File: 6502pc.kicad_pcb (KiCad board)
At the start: 2 copper layers, 32 parts, among them J1 DE9_Receptacle, J2 USB_B, J3 Conn_01x08_Pin, J4 Conn_01x08_Pin, J5 Conn_01x16_Socket, SW1 SW_Push, U1 W65C02SxP, U2 28C256, U3 CY62256-70PC, U4 W65C51NxP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

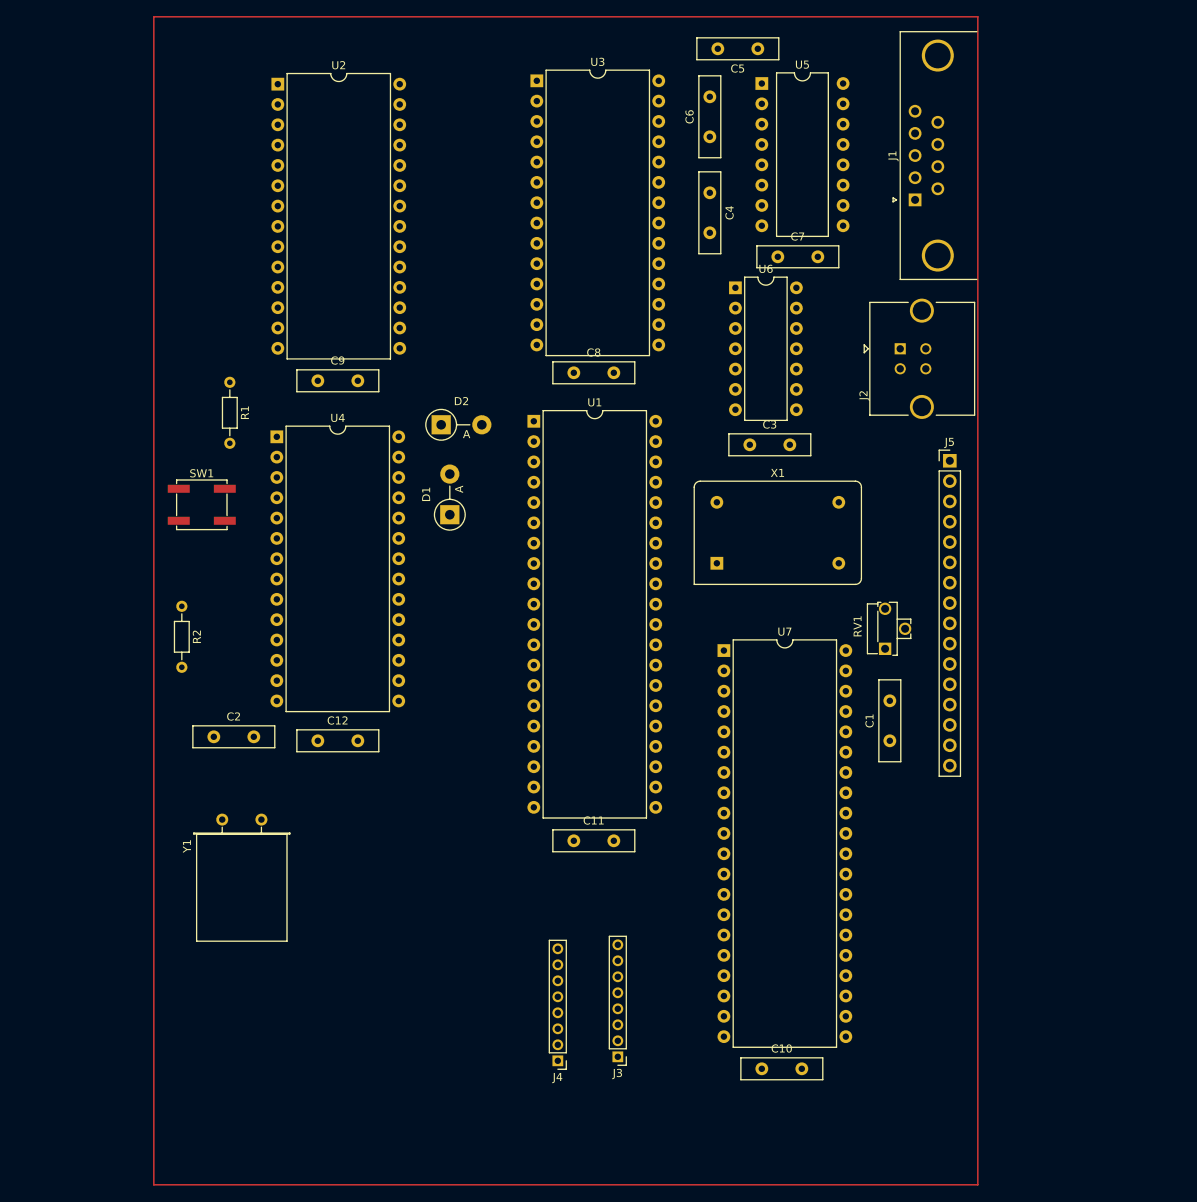
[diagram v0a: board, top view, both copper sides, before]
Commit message: Added Expansion
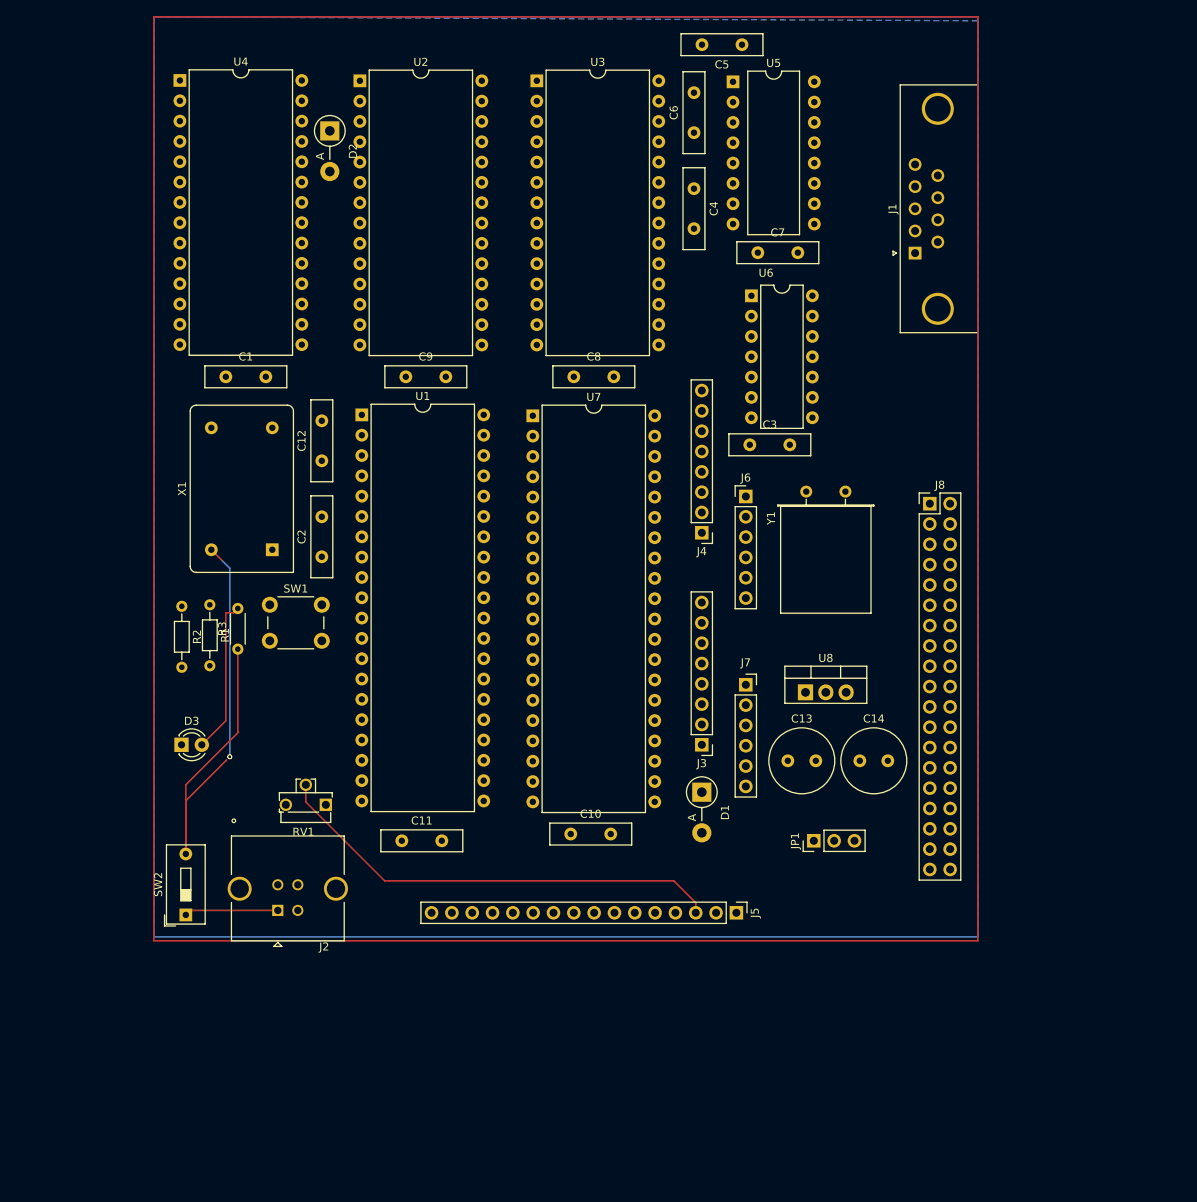
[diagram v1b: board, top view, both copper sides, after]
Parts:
- added C13: 100nF, Capacitor_THT:C_Radial_D8.0mm_H11.5mm_P3.50mm, F.Cu at (114.8, 118.0)
- added C14: 10uF, Capacitor_THT:C_Radial_D8.0mm_H11.5mm_P3.50mm, F.Cu at (123.8, 118.0)
- added D3: LED, LED_THT:LED_D3.0mm, F.Cu at (39.0, 116.0)
- added J6: SD-Card Board, Connector_PinHeader_2.54mm:PinHeader_1x06_P2.54mm_Vertical, F.Cu at (109.5, 85.0)
- added J7: FTDI Socket, Connector_PinSocket_2.54mm:PinSocket_1x06_P2.54mm_Vertical, F.Cu at (109.5, 108.5)
- added J8: Expansion / Diag Port, Connector_PinHeader_2.54mm:PinHeader_2x19_P2.54mm_Vertical, F.Cu at (132.5, 85.9)
- added JP1: SD/FTDI 3.3 or 5v, Connector_PinHeader_2.54mm:PinHeader_1x03_P2.54mm_Vertical, F.Cu at (118.0, 128.0)
- added R3: 220, Resistor_THT:R_Axial_DIN0204_L3.6mm_D1.6mm_P5.08mm_Horizontal, F.Cu at (46.0, 104.0)
- added SW2: SW_SPST, Button_Switch_THT:SW_DIP_SPSTx01_Slide_9.78x4.72mm_W7.62mm_P2.54mm, F.Cu at (39.5, 137.3)
- added U8: LM317_TO-220, Package_TO_SOT_THT:TO-220-3_Vertical, F.Cu at (117.0, 109.4)
- J1: value DE9_Receptacle -> DB9 Serial Port
- J3, J4: footprint Connector_PinHeader_2.00mm:PinHeader_1x08_P2.00mm_Vertical -> Connector_PinHeader_2.54mm:PinHeader_1x08_P2.54mm_Vertical
- SW1: value SW_Push -> Reset Switch; footprint Button_Switch_SMD:SW_SPST_EVPBF -> Button_Switch_THT:SW_PUSH_6mm
- moved J2 104.8 mm to (51.0, 136.7), turned to 180 degrees
- moved C1 94.7 mm to (44.5, 70.0), turned to 0 degrees
- moved Y1 83.7 mm to (117.0, 84.3)
- moved RV1 72.6 mm to (57.0, 123.5), turned to 180 degrees
- moved J4 68.4 mm to (104.0, 89.5)
- moved J5 62.5 mm to (108.3, 137.0), turned to -90 degrees
- moved X1 55.6 mm to (50.3, 91.6), turned to 90 degrees
- moved D1 46.9 mm to (104.0, 121.9), turned to -90 degrees
- moved U4 46.2 mm to (38.8, 33.0)
- moved J3 40.4 mm to (104.0, 116.0)
- moved D2 39.3 mm to (57.5, 39.3), turned to -90 degrees
- moved C10 37.8 mm to (87.6, 127.2)
- moved U7 37.8 mm to (82.9, 74.9)
- moved C12 35.0 mm to (56.5, 80.5), turned to 90 degrees
- moved R1 27.9 mm to (42.5, 98.5)
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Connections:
- net Net-(J4-Pin_2) renamed PA6
- net Net-(J4-Pin_3) renamed PA5
- net Net-(J4-Pin_4) renamed PA4
- net Net-(J4-Pin_5) renamed PA3
- net Net-(J4-Pin_6) renamed PA2
- net Net-(J4-Pin_7) renamed PA1
- net Net-(J4-Pin_8) renamed PA0
- J1 pad 4: unconnected-(J1-Pad4) -> Net-(J7-Pin_6)
- J1 pad 6: unconnected-(J1-Pad6) -> Net-(U4-~{DSR})
- J1 pad 7: unconnected-(J1-Pad7) -> Net-(U4-~{RTS})
- J1 pad 8: unconnected-(J1-Pad8) -> Net-(J7-Pin_2)
- J2 pad 1: VCC -> Net-(J2-VBUS)
- U4 pad 11: unconnected-(U4-~{DTR}-Pad11) -> Net-(J7-Pin_6)
- U4 pad 17: unconnected-(U4-~{DSR}-Pad17) -> Net-(U4-~{DSR})
- U4 pad 8: unconnected-(U4-~{RTS}-Pad8) -> Net-(U4-~{RTS})
- U4 pad 9: unconnected-(U4-~{CTS}-Pad9) -> Net-(J7-Pin_2)
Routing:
- net Net-(J5-Pin_3): track 0.00 -> 57.4 mm
- net VCC: track 0.00 -> 44.1 mm
- net (no net): track 0.00 -> 24.9 mm, vias 0 -> 3
- net Net-(D3-A): track 0.00 -> 19.5 mm
- net Net-(J2-VBUS): track 0.00 -> 11.7 mm
- added copper zone on B.Cu, net GND

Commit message: Added Expansion
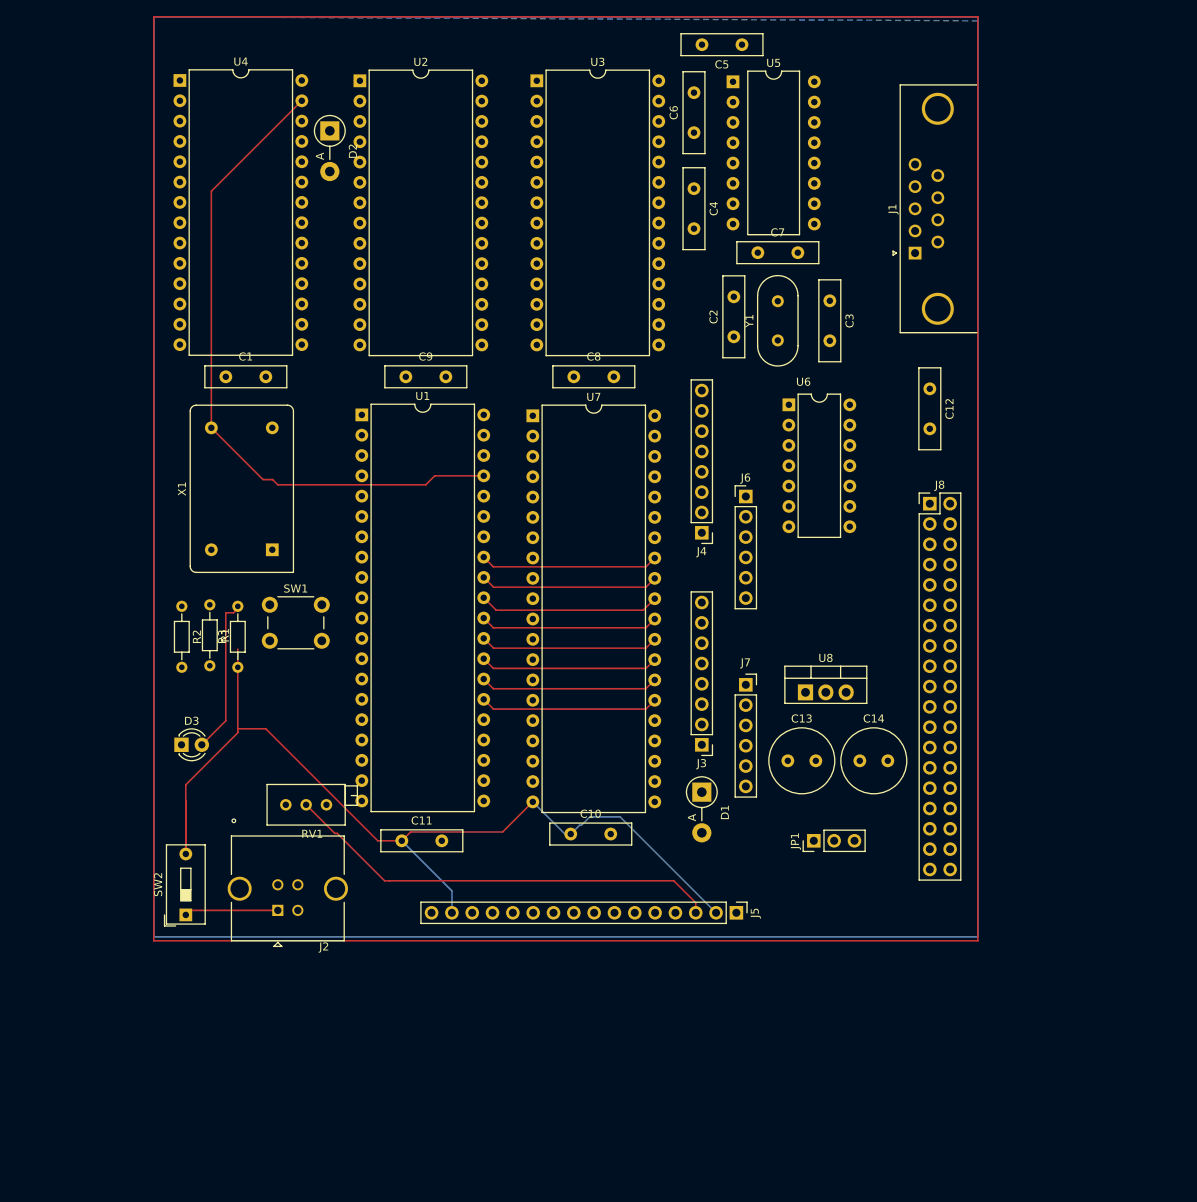
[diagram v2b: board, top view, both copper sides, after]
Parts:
- R3: footprint Resistor_THT:R_Axial_DIN0204_L3.6mm_D1.6mm_P5.08mm_Horizontal -> Resistor_THT:R_Axial_DIN0204_L3.6mm_D1.6mm_P7.62mm_Horizontal
- RV1: footprint Potentiometer_THT:Potentiometer_Runtron_RM-063_Horizontal -> Potentiometer_THT:Potentiometer_Bourns_3296X_Horizontal
- Y1: value Crystal -> 1.8432Mhz; footprint Crystal:Crystal_HC18-U_Horizontal -> Crystal:Crystal_HC18-U_Vertical
- moved C12 76.5 mm to (132.5, 71.5), turned to -90 degrees
- moved C2 58.4 mm to (108.0, 65.0)
- moved C3 20.6 mm to (120.0, 60.5), turned to -90 degrees
- moved Y1 19.2 mm to (113.5, 65.5), turned to 90 degrees
- moved U6 14.4 mm to (114.9, 73.5)
- moved RV1 5.00 mm to (52.0, 123.5)
- moved R3 2.27 mm to (46.0, 106.3)
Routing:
- net clock: track 0.00 -> 83.0 mm
- net VCC: track 44.1 -> 121.7 mm
- net (no net): track 24.9 -> 0.00 mm, vias 3 -> 1
- net D2: track 0.00 -> 22.6 mm
- net D6: track 0.00 -> 22.3 mm
- net D4: track 0.00 -> 22.3 mm
- net D1: track 0.00 -> 22.3 mm
- net D7: track 0.00 -> 22.3 mm
- net D5: track 0.00 -> 22.3 mm
- net D3: track 0.00 -> 22.3 mm
- net D0: track 0.00 -> 22.3 mm
- net Net-(J5-Pin_3): track 57.4 -> 55.0 mm

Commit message: Added Expansion
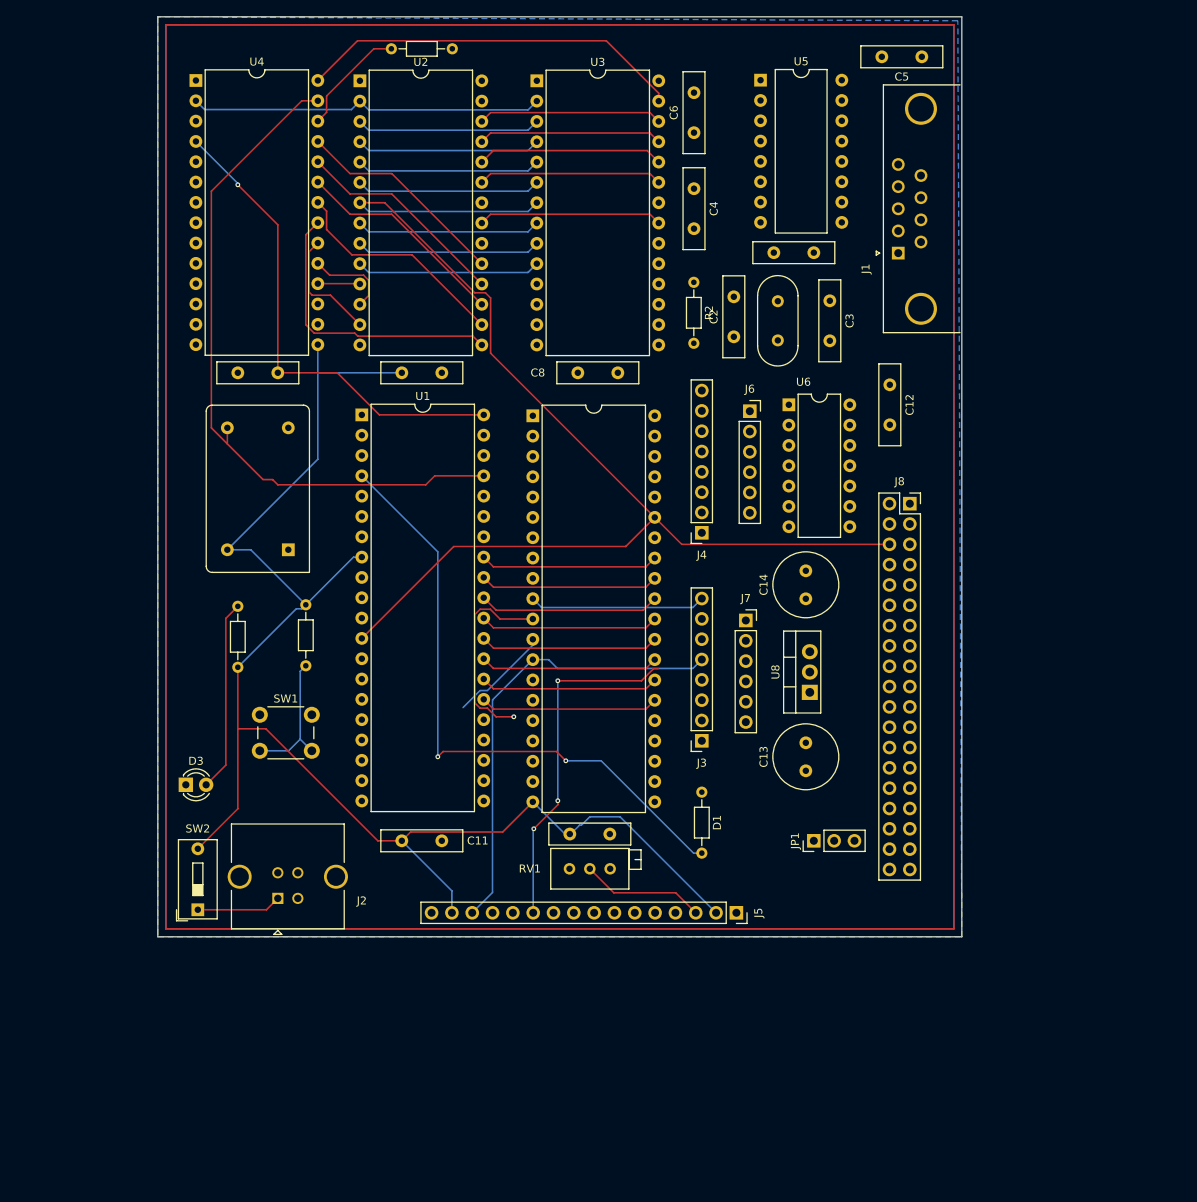
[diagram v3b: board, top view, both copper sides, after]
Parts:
- D1, D2: footprint Diode_THT:D_DO-15_P5.08mm_Vertical_AnodeUp -> Resistor_THT:R_Axial_DIN0204_L3.6mm_D1.6mm_P7.62mm_Horizontal
- J3, J4: footprint Connector_PinHeader_2.54mm:PinHeader_1x08_P2.54mm_Vertical -> Connector_PinSocket_2.54mm:PinSocket_1x08_P2.54mm_Vertical
- J5: footprint Connector_PinHeader_2.54mm:PinHeader_1x16_P2.54mm_Vertical -> Connector_PinSocket_2.54mm:PinSocket_1x16_P2.54mm_Vertical
- J6: footprint Connector_PinHeader_2.54mm:PinHeader_1x06_P2.54mm_Vertical -> Connector_PinSocket_2.54mm:PinSocket_1x06_P2.54mm_Vertical
- J8: footprint Connector_PinHeader_2.54mm:PinHeader_2x19_P2.54mm_Vertical -> Connector_PinSocket_2.54mm:PinSocket_2x19_P2.54mm_Vertical
- moved R2 75.7 mm to (103.0, 58.2)
- moved RV1 36.4 mm to (87.5, 131.5)
- moved C5 22.5 mm to (131.5, 30.0)
- moved C14 21.3 mm to (117.0, 97.8), turned to 90 degrees
- moved SW1 13.8 mm to (48.8, 112.2)
- moved D2 12.8 mm to (65.2, 29.0), turned to 0 degrees
- moved R1 12.0 mm to (54.5, 98.5)
- moved J6 10.7 mm to (110.0, 74.3)
- moved J7 8.04 mm to (109.5, 100.5)
- moved C1 6.52 mm to (51.0, 69.5), turned to 180 degrees
- moved D3 5.03 mm to (39.5, 121.0)
- moved C12 5.02 mm to (127.5, 71.0)
- moved U5 3.45 mm to (111.3, 32.9)
- moved C13 2.57 mm to (117.0, 119.2), turned to 90 degrees
- moved J8 2.50 mm to (130.0, 85.9)
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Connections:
- J3 pad 1: Net-(J3-Pin_1) -> PB7
- J3 pad 2: Net-(J3-Pin_2) -> PB6
- J3 pad 3: Net-(J3-Pin_3) -> PB5
- J3 pad 4: Net-(J3-Pin_4) -> PB4
- J4 pad 1: Net-(J4-Pin_1) -> PA7
- J5 pad 10: unconnected-(J5-Pin_10-Pad10) -> PB3
- J5 pad 11: PB0 -> PB4
- J5 pad 12: PB1 -> PB5
- J5 pad 13: PB2 -> PB6
- J5 pad 14: PB3 -> PB7
- J5 pad 4: PB4 -> PA5
- J5 pad 5: PB5 -> PA6
- J5 pad 6: PB6 -> PA7
- J5 pad 7: unconnected-(J5-Pin_7-Pad7) -> PB0
- J5 pad 8: unconnected-(J5-Pin_8-Pad8) -> PB1
- J5 pad 9: unconnected-(J5-Pin_9-Pad9) -> PB2
- U7 pad 14: Net-(J3-Pin_4) -> PB4
- U7 pad 15: Net-(J3-Pin_3) -> PB5
- U7 pad 16: Net-(J3-Pin_2) -> PB6
- U7 pad 17: Net-(J3-Pin_1) -> PB7
- U7 pad 9: Net-(J4-Pin_1) -> PA7
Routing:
- net A3: track 0.00 -> 153.8 mm
- net Reset: track 0.00 -> 78.3 mm, vias 0 -> 1
- net IRQ: track 0.00 -> 77.6 mm, vias 0 -> 2
- net VCC: track 121.7 -> 186.5 mm
- net PB3: track 0.00 -> 56.8 mm
- net RW: track 0.00 -> 48.4 mm
- net A12: track 0.00 -> 44.4 mm
- net PB4: track 0.00 -> 43.4 mm, vias 0 -> 3
- net Net-(J5-Pin_3): track 55.0 -> 15.5 mm
- net D3: track 22.3 -> 58.8 mm
- net D4: track 22.3 -> 50.5 mm
- net D5: track 22.3 -> 49.2 mm
- net D7: track 22.3 -> 49.2 mm
- net D6: track 22.3 -> 49.2 mm
- net PB1: track 0.00 -> 24.8 mm, vias 0 -> 1
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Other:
- board outline added: 100.5 x 115 mm

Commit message: Added Expansion
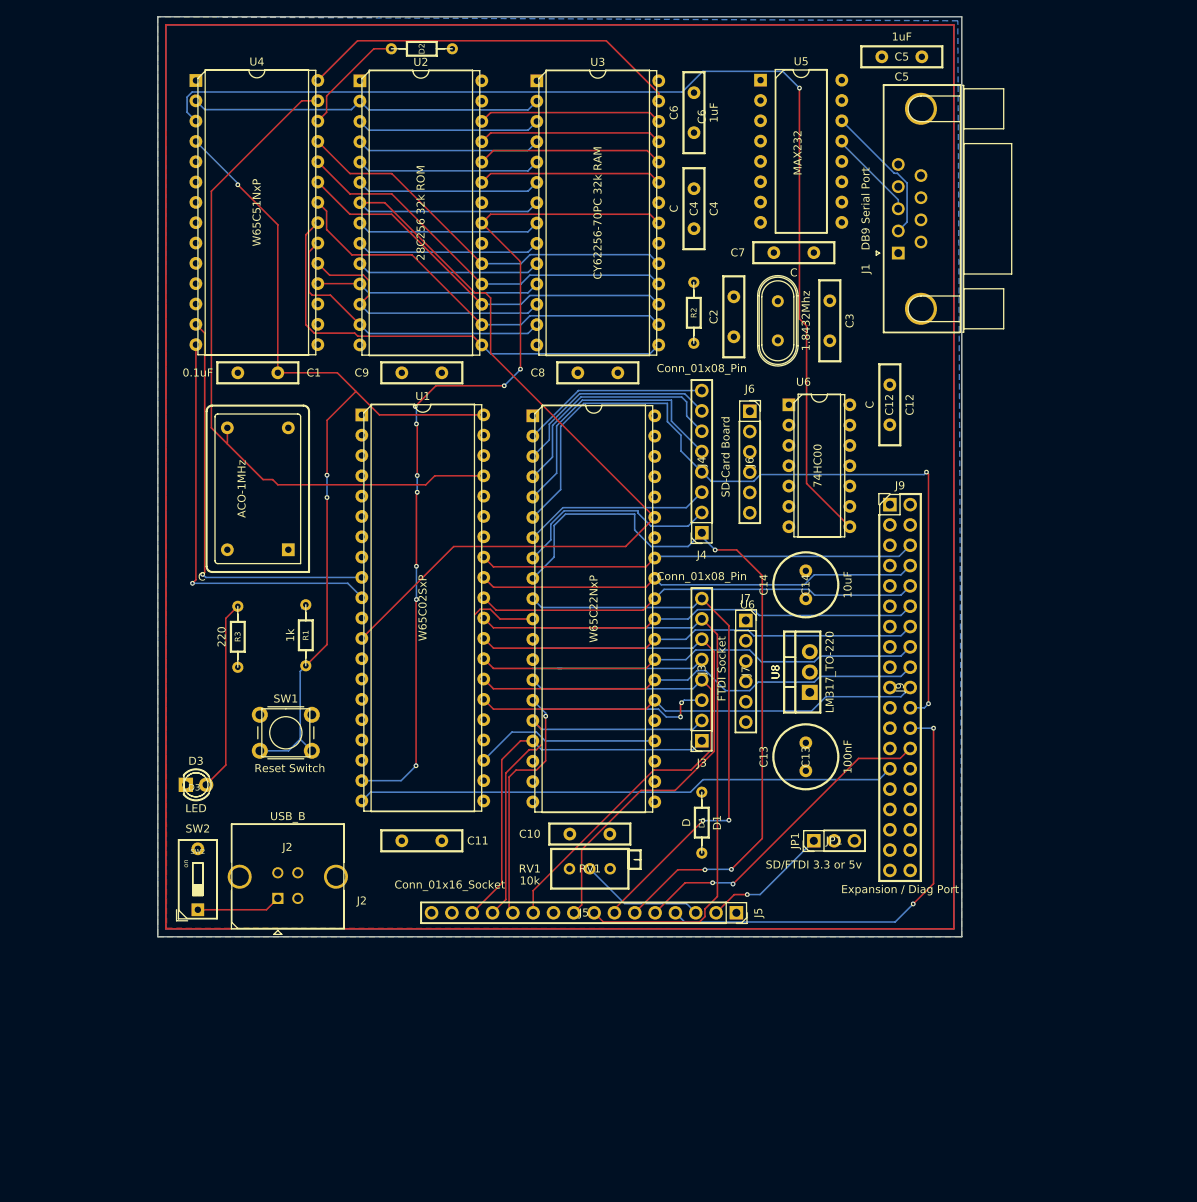
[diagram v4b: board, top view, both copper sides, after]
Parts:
- removed J8: Expansion / Diag Port, Connector_PinSocket_2.54mm:PinSocket_2x19_P2.54mm_Vertical
- added J9: Expansion / Diag Port, Connector_PinHeader_2.54mm:PinHeader_2x19_P2.54mm_Vertical, F.Cu at (127.5, 86.0)
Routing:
- net VCC: track 186.5 -> 17.7 mm, vias 0 -> 1
- net Net-(U4-~{CS2}): track 0.00 -> 139.6 mm, vias 0 -> 1
- net PA4: track 0.00 -> 98.3 mm, vias 0 -> 2
- net PA7: track 0.00 -> 93.0 mm, vias 0 -> 3
- net A10: track 23.0 -> 111.0 mm, vias 0 -> 9
- net PA5: track 0.00 -> 80.6 mm, vias 0 -> 2
- net IRQ: track 77.6 -> 0.00 mm, vias 2 -> 0
- net A11: track 23.0 -> 90.7 mm
- net PA6: track 0.00 -> 66.9 mm, vias 0 -> 2
- net D6: track 49.2 -> 106.9 mm
- net PB1: track 24.8 -> 81.8 mm, vias 1 -> 0
- net D5: track 49.2 -> 106.0 mm
- net D7: track 49.2 -> 105.9 mm
- net D1: track 33.0 -> 89.3 mm
- net D3: track 58.8 -> 115.0 mm
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- added copper zone on F.Cu, net VCC
